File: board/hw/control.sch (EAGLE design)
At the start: 38 parts, among them T1 pn2222a, T2 pn2222a, T3 pn2222a, T4 pn2222a, T5 pn2222a, T6 pn2222a, T7 pn2222a, T8 pn2222a

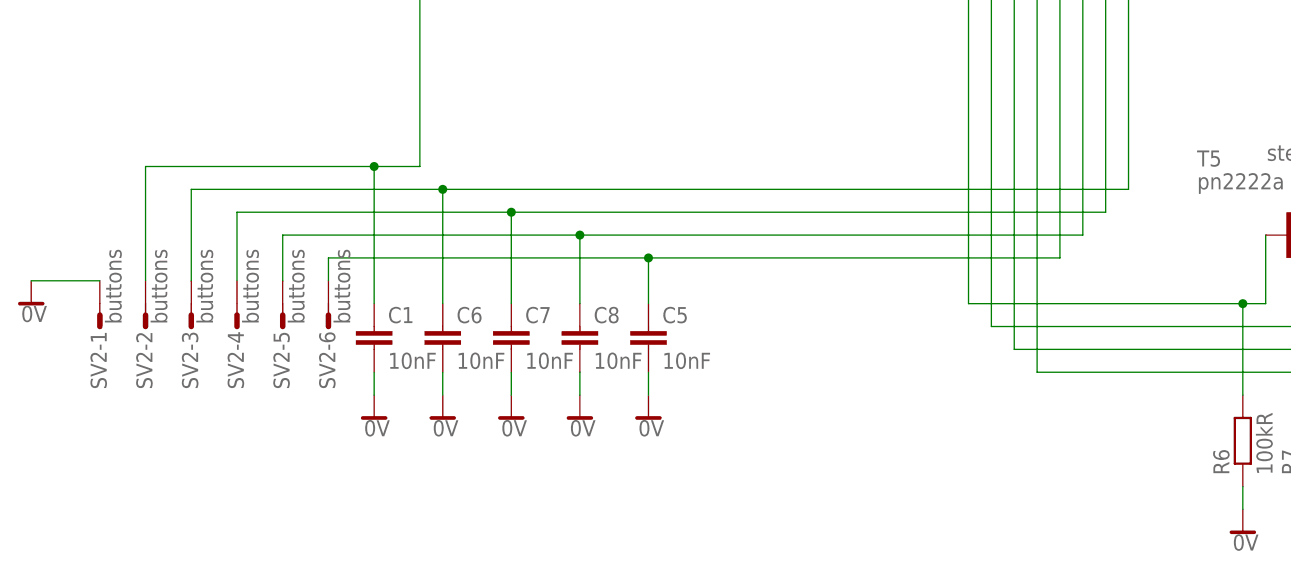
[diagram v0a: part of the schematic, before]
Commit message: removed capacitors for buttons - these are already covered by the external board
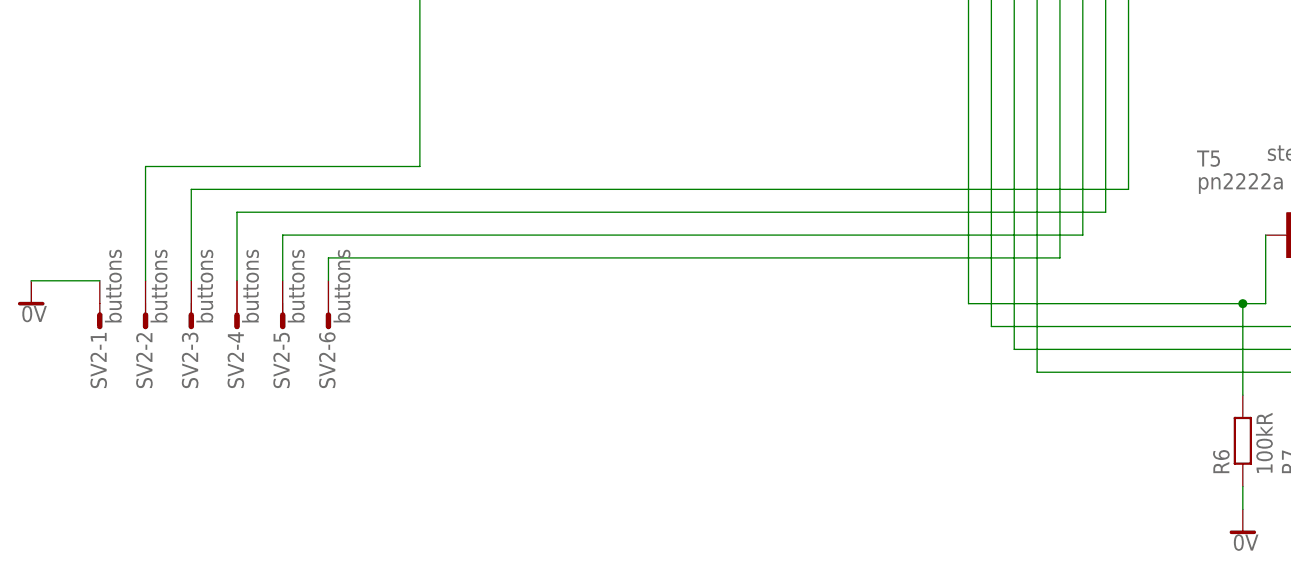
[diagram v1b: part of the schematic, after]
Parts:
- removed C1, C5, C6, C7, C8: 10nF, rcl:C-EUC0805K
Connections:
- net 0V: no longer C1.2, C5.2, C6.2, C7.2, C8.2
- net N$22: no longer C8.1
- net N$23: no longer C7.1
- net N$24: no longer C6.1
- net N$25: no longer C1.1
- net N$3: no longer C5.1

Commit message: single-layer routing completed (yay)
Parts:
- added D9: 1N4446, diode:1N4446
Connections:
- new net N$26: C3.+, C4.2, D9.C, U$1.VCC
- net +5V: now also D9.A; no longer C3.+, C4.2, U$1.VCC
- net N$11: now also U$1.(AIN1)PB1; no longer U$1.(OC0A)PB2
- net N$13: now also U$1.(OC0A)PB2; no longer U$1.(AIN1)PB1
- net N$15: now also U$1.(OC1A)PB3; no longer U$1.(AIN0)PB0
- net N$18: now also U$1.(INT0)PD2; no longer U$1.(INT1)PD3
- net N$6: now also U$1.(INT1)PD3; no longer U$1.(INT0)PD2
- net N$9: now also U$1.(AIN0)PB0; no longer U$1.(OC1A)PB3
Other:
- moved on the sheet: C3, C4
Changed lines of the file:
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@@
 <parts>
 <part name="U$1" library="avr-7" deviceset="TINY2313*" device="-*P*" value="TINY2313"/>
-<part name="SUPPLY2" library="supply2" deviceset="+5V" device=""/>
 <part name="SUPPLY5" library="supply2" deviceset="0V" device=""/>
 <part name="C3" library="rcl" deviceset="CPOL-EU" device="153CLV-0405" value="4.7uF"/>
@@
 <part name="SV2" library="con-amp-mt" deviceset="S06P" device="" value="buttons"/>
 <part name="SUPPLY40" library="supply2" deviceset="0V" device=""/>
+<part name="D9" library="diode" deviceset="1N4446" device=""/>
 </parts>
 <sheets>
@@
 <instances>
 <instance part="U$1" gate="G$1" x="63.5" y="58.42"/>
-<instance part="SUPPLY2" gate="+5V" x="40.64" y="40.64"/>
 <instance part="SUPPLY5" gate="0V" x="40.64" y="27.94"/>
-<instance part="C3" gate="G$1" x="10.16" y="35.56"/>
-<instance part="SUPPLY15" gate="+5V" x="10.16" y="43.18"/>
-<instance part="SUPPLY16" gate="0V" x="10.16" y="25.4"/>
-<instance part="SUPPLY17" gate="0V" x="27.94" y="35.56"/>
+<instance part="C3" gate="G$1" x="-2.54" y="35.56"/>
+<instance part="SUPPLY15" gate="+5V" x="-7.62" y="55.88"/>
+<instance part="SUPPLY16" gate="0V" x="-2.54" y="25.4"/>
+<instance part="SUPPLY17" gate="0V" x="12.7" y="25.4"/>
 <instance part="T1" gate="G$1" x="121.92" y="71.12"/>
 <instance part="SUPPLY19" gate="+5V" x="124.46" y="93.98"/>
 <instance part="SUPPLY20" gate="0V" x="127" y="63.5"/>
-<instance part="C4" gate="G$1" x="33.02" y="38.1" rot="R90"/>
+<instance part="C4" gate="G$1" x="12.7" y="33.02" rot="R180"/>
 <instance part="T2" gate="G$1" x="149.86" y="71.12"/>
 <instance part="SUPPLY21" gate="+5V" x="152.4" y="93.98"/>
@@
 <instance part="SV2" gate="-6" x="12.7" y="-22.86" rot="R90"/>
 <instance part="SUPPLY40" gate="0V" x="-20.32" y="-20.32"/>
+<instance part="D9" gate="1" x="-5.08" y="48.26"/>
 </instances>
 <busses>
@@
 <net name="+5V" class="0">
 <segment>
-<wire x1="10.16" y1="40.64" x2="10.16" y2="38.1" width="0.1524" layer="91"/>
-<pinref part="C3" gate="G$1" pin="+"/>
-<pinref part="SUPPLY15" gate="+5V" pin="+5V"/>
-</segment>
-<segment>
-<wire x1="38.1" y1="38.1" x2="40.64" y2="38.1" width="0.1524" layer="91"/>
-<wire x1="40.64" y1="38.1" x2="43.18" y2="38.1" width="0.1524" layer="91"/>
-<junction x="40.64" y="38.1"/>
-<pinref part="SUPPLY2" gate="+5V" pin="+5V"/>
-<pinref part="U$1" gate="G$1" pin="VCC"/>
-<pinref part="C4" gate="G$1" pin="2"/>
-</segment>
-<segment>
 <wire x1="30.48" y1="86.36" x2="22.86" y2="86.36" width="0.1524" layer="91"/>
 <pinref part="SV1" gate="G$1" pin="2"/>
@@
 <wire x1="124.46" y1="91.44" x2="124.46" y2="83.82" width="0.1524" layer="91"/>
 </segment>
+<segment>
+<pinref part="D9" gate="1" pin="A"/>
+<pinref part="SUPPLY15" gate="+5V" pin="+5V"/>
+<wire x1="-7.62" y1="53.34" x2="-7.62" y2="48.26" width="0.1524" layer="91"/>
+</segment>
 </net>
 <net name="0V" class="0">
@@
 </segment>
 <segment>
-<wire x1="10.16" y1="27.94" x2="10.16" y2="30.48" width="0.1524" layer="91"/>
+<wire x1="-2.54" y1="27.94" x2="-2.54" y2="30.48" width="0.1524" layer="91"/>
 <pinref part="C3" gate="G$1" pin="-"/>
 <pinref part="SUPPLY16" gate="0V" pin="0V"/>
 </segment>
 <segment>
-<wire x1="27.94" y1="38.1" x2="30.48" y2="38.1" width="0.1524" layer="91"/>
+<wire x1="12.7" y1="27.94" x2="12.7" y2="30.48" width="0.1524" layer="91"/>
 <pinref part="SUPPLY17" gate="0V" pin="0V"/>
 <pinref part="C4" gate="G$1" pin="1"/>
@@
 <net name="N$9" class="0">
 <segment>
-<wire x1="81.28" y1="63.5" x2="116.84" y2="63.5" width="0.1524" layer="91"/>
 <wire x1="116.84" y1="63.5" x2="119.38" y2="63.5" width="0.1524" layer="91"/>
 <wire x1="119.38" y1="63.5" x2="119.38" y2="71.12" width="0.1524" layer="91"/>
 <wire x1="116.84" y1="53.34" x2="116.84" y2="63.5" width="0.1524" layer="91"/>
-<junction x="116.84" y="63.5"/>
-<pinref part="U$1" gate="G$1" pin="(OC1A)PB3"/>
 <pinref part="T1" gate="G$1" pin="B"/>
 <pinref part="R1" gate="G$1" pin="2"/>
+<pinref part="U$1" gate="G$1" pin="(AIN0)PB0"/>
+<wire x1="81.28" y1="55.88" x2="91.44" y2="55.88" width="0.1524" layer="91"/>
+<wire x1="91.44" y1="55.88" x2="91.44" y2="50.8" width="0.1524" layer="91"/>
+<wire x1="91.44" y1="50.8" x2="111.76" y2="50.8" width="0.1524" layer="91"/>
+<wire x1="111.76" y1="50.8" x2="111.76" y2="63.5" width="0.1524" layer="91"/>
+<wire x1="111.76" y1="63.5" x2="116.84" y2="63.5" width="0.1524" layer="91"/>
+<junction x="116.84" y="63.5"/>
 </segment>
 </net>
@@
 <segment>
 <wire x1="147.32" y1="60.96" x2="147.32" y2="71.12" width="0.1524" layer="91"/>
-<wire x1="81.28" y1="60.96" x2="124.46" y2="60.96" width="0.1524" layer="91"/>
 <wire x1="124.46" y1="60.96" x2="147.32" y2="60.96" width="0.1524" layer="91"/>
 <wire x1="124.46" y1="53.34" x2="124.46" y2="60.96" width="0.1524" layer="91"/>
+<pinref part="T2" gate="G$1" pin="B"/>
+<pinref part="R3" gate="G$1" pin="2"/>
+<pinref part="U$1" gate="G$1" pin="(AIN1)PB1"/>
+<wire x1="81.28" y1="58.42" x2="93.98" y2="58.42" width="0.1524" layer="91"/>
+<wire x1="93.98" y1="58.42" x2="93.98" y2="53.34" width="0.1524" layer="91"/>
+<wire x1="93.98" y1="53.34" x2="114.3" y2="53.34" width="0.1524" layer="91"/>
+<wire x1="114.3" y1="53.34" x2="114.3" y2="60.96" width="0.1524" layer="91"/>
+<wire x1="114.3" y1="60.96" x2="124.46" y2="60.96" width="0.1524" layer="91"/>
 <junction x="124.46" y="60.96"/>
-<pinref part="T2" gate="G$1" pin="B"/>
-<pinref part="U$1" gate="G$1" pin="(OC0A)PB2"/>
-<pinref part="R3" gate="G$1" pin="2"/>
 </segment>
 </net>
@@
 <segment>
 <wire x1="175.26" y1="58.42" x2="175.26" y2="71.12" width="0.1524" layer="91"/>
-<wire x1="81.28" y1="58.42" x2="132.08" y2="58.42" width="0.1524" layer="91"/>
 <wire x1="132.08" y1="58.42" x2="175.26" y2="58.42" width="0.1524" layer="91"/>
 <wire x1="132.08" y1="53.34" x2="132.08" y2="58.42" width="0.1524" layer="91"/>
+<pinref part="T3" gate="G$1" pin="B"/>
+<pinref part="R4" gate="G$1" pin="2"/>
+<pinref part="U$1" gate="G$1" pin="(OC0A)PB2"/>
+<wire x1="81.28" y1="60.96" x2="96.52" y2="60.96" width="0.1524" layer="91"/>
+<wire x1="96.52" y1="60.96" x2="96.52" y2="58.42" width="0.1524" layer="91"/>
+<wire x1="96.52" y1="58.42" x2="132.08" y2="58.42" width="0.1524" layer="91"/>
 <junction x="132.08" y="58.42"/>
-<pinref part="T3" gate="G$1" pin="B"/>
-<pinref part="U$1" gate="G$1" pin="(AIN1)PB1"/>
-<pinref part="R4" gate="G$1" pin="2"/>
 </segment>
 </net>
@@
 <net name="N$15" class="0">
 <segment>
-<wire x1="81.28" y1="55.88" x2="139.7" y2="55.88" width="0.1524" layer="91"/>
 <wire x1="139.7" y1="55.88" x2="203.2" y2="55.88" width="0.1524" layer="91"/>
 <wire x1="203.2" y1="55.88" x2="203.2" y2="71.12" width="0.1524" layer="91"/>
 <wire x1="139.7" y1="53.34" x2="139.7" y2="55.88" width="0.1524" layer="91"/>
+<pinref part="T4" gate="G$1" pin="B"/>
+<pinref part="R5" gate="G$1" pin="2"/>
+<pinref part="U$1" gate="G$1" pin="(OC1A)PB3"/>
+<wire x1="81.28" y1="63.5" x2="99.06" y2="63.5" width="0.1524" layer="91"/>
+<wire x1="99.06" y1="63.5" x2="99.06" y2="55.88" width="0.1524" layer="91"/>
+<wire x1="99.06" y1="55.88" x2="139.7" y2="55.88" width="0.1524" layer="91"/>
 <junction x="139.7" y="55.88"/>
-<pinref part="T4" gate="G$1" pin="B"/>
-<pinref part="U$1" gate="G$1" pin="(AIN0)PB0"/>
-<pinref part="R5" gate="G$1" pin="2"/>
 </segment>
 </net>
@@
 <pinref part="T7" gate="G$1" pin="B"/>
 <pinref part="R8" gate="G$1" pin="2"/>
-<pinref part="U$1" gate="G$1" pin="(INT0)PD2"/>
-<wire x1="81.28" y1="35.56" x2="88.9" y2="35.56" width="0.1524" layer="91"/>
-<wire x1="88.9" y1="35.56" x2="88.9" y2="-25.4" width="0.1524" layer="91"/>
+<wire x1="88.9" y1="38.1" x2="88.9" y2="-25.4" width="0.1524" layer="91"/>
 <wire x1="88.9" y1="-25.4" x2="129.54" y2="-25.4" width="0.1524" layer="91"/>
 <junction x="129.54" y="-25.4"/>
+<pinref part="U$1" gate="G$1" pin="(INT1)PD3"/>
+<wire x1="81.28" y1="38.1" x2="88.9" y2="38.1" width="0.1524" layer="91"/>
 </segment>
 </net>
@@
 <pinref part="T8" gate="G$1" pin="B"/>
 <pinref part="R9" gate="G$1" pin="2"/>
-<pinref part="U$1" gate="G$1" pin="(INT1)PD3"/>
-<wire x1="81.28" y1="38.1" x2="91.44" y2="38.1" width="0.1524" layer="91"/>
-<wire x1="91.44" y1="38.1" x2="91.44" y2="-27.94" width="0.1524" layer="91"/>
+<wire x1="91.44" y1="35.56" x2="91.44" y2="-27.94" width="0.1524" layer="91"/>
 <wire x1="91.44" y1="-27.94" x2="137.16" y2="-27.94" width="0.1524" layer="91"/>
 <junction x="137.16" y="-27.94"/>
+<pinref part="U$1" gate="G$1" pin="(INT0)PD2"/>
+<wire x1="91.44" y1="35.56" x2="81.28" y2="35.56" width="0.1524" layer="91"/>
 </segment>
 </net>
@@
 </segment>
 </net>
+<net name="N$26" class="0">
+<segment>
+<wire x1="12.7" y1="38.1" x2="43.18" y2="38.1" width="0.1524" layer="91"/>
+<pinref part="U$1" gate="G$1" pin="VCC"/>
+<pinref part="C4" gate="G$1" pin="2"/>
+<pinref part="C3" gate="G$1" pin="+"/>
+<wire x1="12.7" y1="38.1" x2="-2.54" y2="38.1" width="0.1524" layer="91"/>
+<wire x1="-2.54" y1="38.1" x2="-2.54" y2="48.26" width="0.1524" layer="91"/>
+<pinref part="D9" gate="1" pin="C"/>
+<junction x="-2.54" y="38.1"/>
+<junction x="12.7" y="38.1"/>
+</segment>
+</net>
 </nets>
 </sheet>
 </sheets>
+<errors>
+</errors>
 </schematic>
 </drawing>

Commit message: added missing power supply connector
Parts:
- added SV3: (no value), con-amp-mt:S02P
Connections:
- net +5V: now also SV3-1.S
- net 0V: now also SV3-2.S
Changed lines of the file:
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@@
 <part name="SUPPLY40" library="supply2" deviceset="0V" device=""/>
 <part name="D9" library="diode" deviceset="1N4446" device=""/>
+<part name="SV3" library="con-amp-mt" deviceset="S02P" device=""/>
+<part name="SUPPLY2" library="supply2" deviceset="+5V" device=""/>
+<part name="SUPPLY41" library="supply2" deviceset="0V" device=""/>
 </parts>
 <sheets>
@@
 <instance part="SUPPLY40" gate="0V" x="-20.32" y="-20.32"/>
 <instance part="D9" gate="1" x="-5.08" y="48.26"/>
+<instance part="SV3" gate="-1" x="-20.32" y="91.44"/>
+<instance part="SV3" gate="-2" x="-20.32" y="86.36"/>
+<instance part="SUPPLY2" gate="+5V" x="-12.7" y="93.98"/>
+<instance part="SUPPLY41" gate="0V" x="-12.7" y="83.82"/>
 </instances>
 <busses>
@@
 <wire x1="-7.62" y1="53.34" x2="-7.62" y2="48.26" width="0.1524" layer="91"/>
 </segment>
+<segment>
+<pinref part="SV3" gate="-1" pin="S"/>
+<pinref part="SUPPLY2" gate="+5V" pin="+5V"/>
+<wire x1="-12.7" y1="91.44" x2="-15.24" y2="91.44" width="0.1524" layer="91"/>
+</segment>
 </net>
 <net name="0V" class="0">
@@
 <wire x1="-12.7" y1="-17.78" x2="-20.32" y2="-17.78" width="0.1524" layer="91"/>
 </segment>
+<segment>
+<pinref part="SV3" gate="-2" pin="S"/>
+<pinref part="SUPPLY41" gate="0V" pin="0V"/>
+<wire x1="-12.7" y1="86.36" x2="-15.24" y2="86.36" width="0.1524" layer="91"/>
+</segment>
 </net>
